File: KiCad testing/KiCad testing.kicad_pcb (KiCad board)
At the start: 2 copper layers, 29 parts, among them J1 USB_A, Q1 IRF540N, Q2 IRF540N, Q3 IRF540N, U1 IR2113S, U2 IR2113S, U3 ACS712xLCTR-05B

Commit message: Update Schematic
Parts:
- removed U2: IR2113S, Package_DIP:DIP-14_W7.62mm_Socket
- added C1: 10uF, Capacitor_THT:CP_Radial_D5.0mm_P2.00mm, F.Cu at (72.9, 149.9)
- added C2: 10uF, Capacitor_THT:CP_Radial_D5.0mm_P2.00mm, F.Cu at (61.5, 144.1)
- added C3: 100uF, Capacitor_THT:CP_Radial_D6.3mm_P2.50mm, F.Cu at (48.8, 140.2)
- added C4: 100nF, Capacitor_THT:C_Disc_D4.7mm_W2.5mm_P5.00mm, F.Cu at (45.1, 133.9)
- added C5: 10uF, Capacitor_THT:CP_Radial_D5.0mm_P2.00mm, F.Cu at (107.9, 151.1)
- added C6: 10uF, Capacitor_THT:CP_Radial_D5.0mm_P2.00mm, F.Cu at (95.9, 143.5)
- added C7: 100uF, Capacitor_THT:CP_Radial_D6.3mm_P2.50mm, F.Cu at (83.8, 139.7)
- added C8: 100nF, Capacitor_THT:C_Disc_D4.7mm_W2.5mm_P5.00mm, F.Cu at (80.7, 133.3)
- added U4: IR2213, Package_DIP:DIP-14_W7.62mm, F.Cu at (67.8, 129.5)
- U1: value IR2113S -> IR2213; footprint Package_DIP:DIP-14_W7.62mm_Socket -> Package_DIP:DIP-14_W7.62mm
- moved J1 149.3 mm to (49.7, 105.5), turned to -90 degrees
- moved R6 110.6 mm to (99.0, 148.6), turned to 180 degrees
- moved R3 108.1 mm to (64.0, 149.1), turned to 180 degrees
- moved C11 106.1 mm to (85.6, 160.0)
- moved C12 106.1 mm to (105.9, 162.5)
- moved D5 106.1 mm to (100.8, 167.7)
- moved L2 106.1 mm to (95.8, 161.3)
- moved Q1 106.1 mm to (98.3, 172.8)
- moved C9 103.6 mm to (71.6, 161.3)
- moved D3 103.6 mm to (56.4, 167.6)
- moved D4 103.6 mm to (70.3, 167.6)
- moved C10 103.6 mm to (51.1, 158.8)
- moved L1 103.6 mm to (62.7, 158.8)
- moved Q2 103.6 mm to (67.8, 172.7)
- moved Q3 103.6 mm to (53.8, 172.7)
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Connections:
- A1 pad 12: PWM_High -> PWM_Low
- A1 pad 13: PWM_Low -> PWM_High
- R1 pad 2: Net-(U1-LO) -> Net-(U4-LO)
- R3 pad 1: Net-(U1-HO) -> Net-(U4-HO)
- R4 pad 2: Net-(U2-LO) -> Net-(U1-LO)
- R6 pad 1: Net-(U2-HO) -> Net-(U1-HO)
- U1 pad 10: unconnected-(U1-NC-Pad10) -> PWM_MPPT
- U1 pad 11: 5V -> +Buck_Boost_Load
- U1 pad 12: PWM_High -> unconnected-(U1-LIN-Pad12)
- U1 pad 14: PWM_Low -> unconnected-(U1-NC-Pad14)
- U1 pad 5: unconnected-(U1-NC-Pad5) -> VS_1
- U1 pad 6: VS -> Net-(D2-K)
- U1 pad 7: Net-(D1-K) -> Net-(U1-HO)
- U1 pad 8: Net-(U1-HO) -> unconnected-(U1-NC-Pad8)
- U1 pad 9: unconnected-(U1-NC-Pad9) -> 5V
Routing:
- net +Buck_Boost_Load: track 60.7 -> 216.8 mm
- net 5V: track 0.00 -> 100.5 mm
- net 12V: track 7.86 -> 76.8 mm
- net PWM_MPPT: track 0.00 -> 37.4 mm
- net PWM_High: track 0.00 -> 28.1 mm
- net Gate_High: track 67.6 -> 39.5 mm
- net Gate_High_1: track 64.8 -> 38.2 mm
- net PWM_Low: track 0.00 -> 22.0 mm
- net Net-(D1-K): track 15.5 -> 33.3 mm
- net Net-(D2-K): track 15.2 -> 31.5 mm
- net VS_1: track 3.82 -> 12.0 mm
- net VS: track 48.3 -> 54.2 mm
- net Net-(U2-LO): track 5.25 -> 0.00 mm
- net Net-(U4-LO): track 0.00 -> 5.16 mm
- net Net-(U2-HO): track 3.80 -> 0.00 mm
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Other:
- board outline added: 101.6 x 127 mm
- board text added: "Cut outline marks the biggest pcb craftable."

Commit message: Update Schematic
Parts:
- C2, C6: value 10uF -> 470uF; footprint Capacitor_THT:CP_Radial_D5.0mm_P2.00mm -> Capacitor_THT:CP_Radial_D10.0mm_P5.00mm

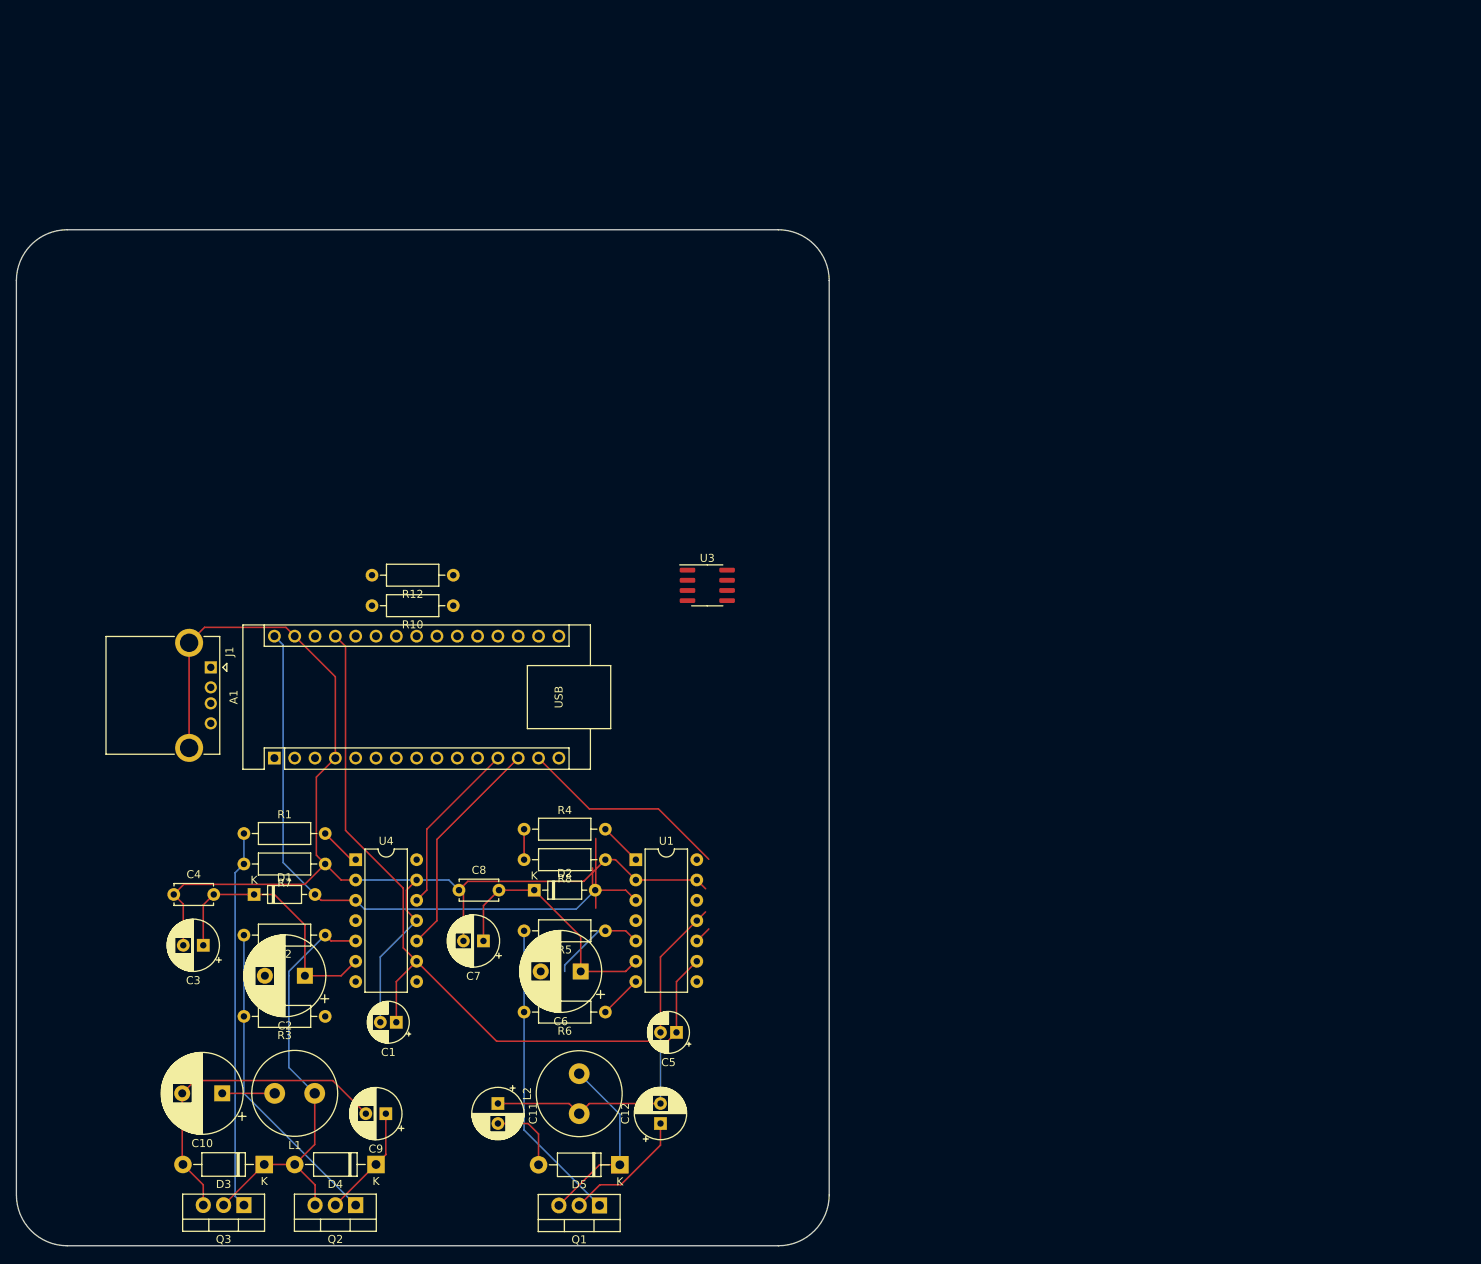
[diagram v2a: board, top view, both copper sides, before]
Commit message: Update schematic and redesign pcb layout.
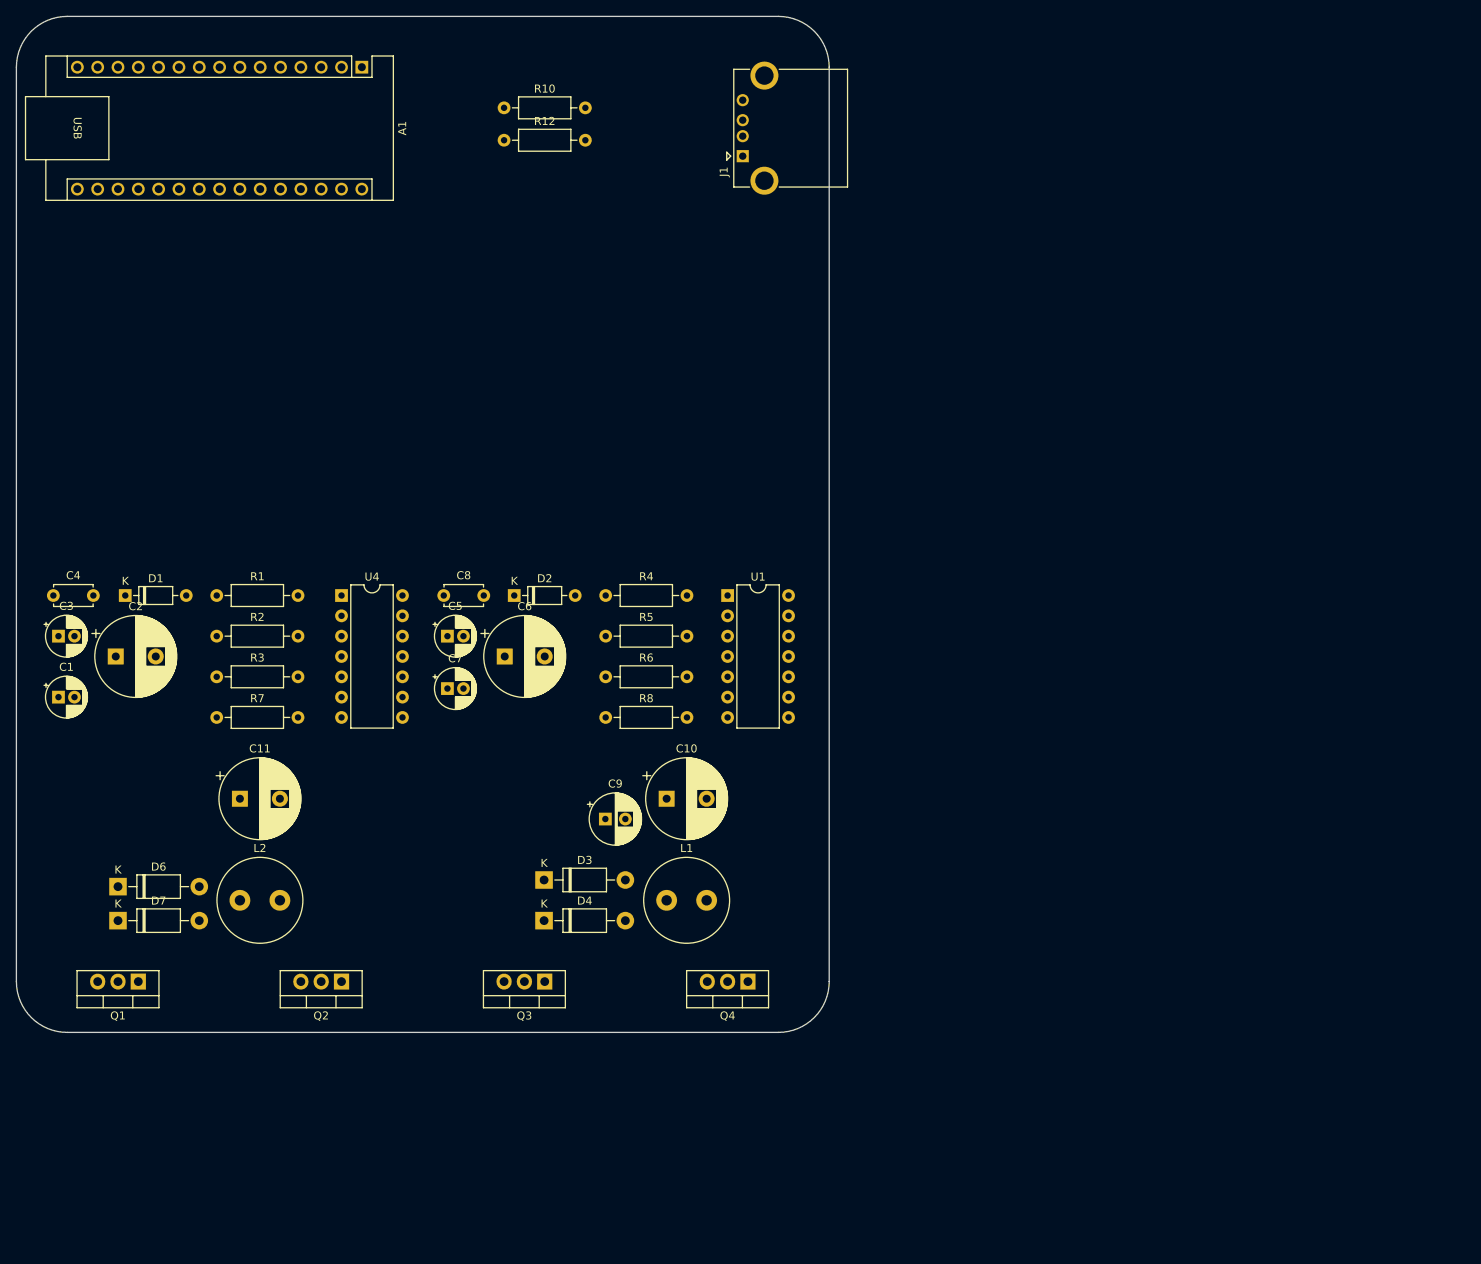
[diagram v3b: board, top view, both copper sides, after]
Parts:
- removed C12: 47uF, Capacitor_THT:CP_Radial_D6.3mm_P2.50mm
- removed D5: 1N4002, Diode_THT:D_DO-41_SOD81_P10.16mm_Horizontal
- removed U3: ACS712xLCTR-05B, Package_SO:SOIC-8_3.9x4.9mm_P1.27mm
- added D6: 1N4002, Diode_THT:D_DO-41_SOD81_P10.16mm_Horizontal, F.Cu at (38.1, 132.9)
- added D7: 1N4002, Diode_THT:D_DO-41_SOD81_P10.16mm_Horizontal, F.Cu at (38.1, 137.2)
- added Q4: IRF540N, Package_TO_SOT_THT:TO-220-3_Vertical, F.Cu at (116.8, 144.8)
- C11: value 47uF -> 1000uF; footprint Capacitor_THT:CP_Radial_D6.3mm_P2.50mm -> Capacitor_THT:CP_Radial_D10.0mm_P5.00mm
- C3, C7: footprint Capacitor_THT:CP_Radial_D6.3mm_P2.50mm -> Capacitor_THT:CP_Radial_D5.0mm_P2.00mm
- moved J1 92.2 mm to (116.2, 41.6), turned to 90 degrees
- moved A1 87.0 mm to (68.6, 30.5), turned to -90 degrees
- moved C10 66.7 mm to (106.7, 121.9), turned to 0 degrees
- moved Q1 64.1 mm to (40.6, 144.8)
- moved R10 62.6 mm to (86.4, 35.6), turned to 0 degrees
- moved C1 58.6 mm to (30.7, 109.2), turned to 0 degrees
- moved C5 57.2 mm to (79.3, 101.6), turned to 0 degrees
- moved R12 54.7 mm to (86.4, 39.6), turned to 0 degrees
- moved L1 50.2 mm to (106.7, 134.6), turned to 0 degrees
- moved L2 50.1 mm to (53.3, 134.6), turned to 0 degrees
- moved C11 49.9 mm to (53.3, 121.9), turned to 0 degrees
- moved D3 49.9 mm to (91.4, 132.1), turned to 0 degrees
- moved Q3 46.8 mm to (91.4, 144.8)
- moved C2 46.4 mm to (37.8, 104.1), turned to 0 degrees
- moved C9 45.9 mm to (99.0, 124.5), turned to 0 degrees
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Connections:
- A1 pad 29: +Buck_Boost_Load -> GND
- A1 pad 4: +Buck_Boost_Load -> GND
- C1 pad 2: +Buck_Boost_Load -> GND
- C11 pad 1: +Buck_Boost_Load -> -DCDC_Load
- C11 pad 2: -Buck_Boost_Load -> +DCDC_Load
- C3 pad 2: +Buck_Boost_Load -> GND
- C4 pad 1: +Buck_Boost_Load -> GND
- C5 pad 2: +Buck_Boost_Load -> GND
- C7 pad 2: +Buck_Boost_Load -> GND
- C8 pad 1: +Buck_Boost_Load -> GND
- J1 pad 5: +Buck_Boost_Load -> GND
- L2 pad 1: +Buck_Boost_Load -> Net-(D6-K)
- L2 pad 2: Net-(D5-K) -> Net-(D7-A)
- Q1 pad 3: Net-(D5-K) -> Net-(D6-K)
- Q2 pad 1: Gate_High -> Gate_Low_1
- Q2 pad 2: -Bidirectional_DCDC_Load -> Net-(D7-A)
- Q2 pad 3: VS -> -DCDC_Load
- Q3 pad 1: Gate_Low -> Gate_High
- Q3 pad 2: VS -> -Bidirectional_DCDC_Load
- Q3 pad 3: +Bidirectional_DCDC_Load -> VS
- R10 pad 2: +Buck_Boost_Load -> GND
- R12 pad 2: +Buck_Boost_Load -> GND
- R7 pad 1: +Buck_Boost_Load -> GND
- R8 pad 1: +Buck_Boost_Load -> GND
- U1 pad 11: +Buck_Boost_Load -> GND
- U1 pad 13: +Buck_Boost_Load -> GND
- U1 pad 2: +Buck_Boost_Load -> GND
- U4 pad 11: +Buck_Boost_Load -> GND
- U4 pad 13: +Buck_Boost_Load -> GND
- U4 pad 2: +Buck_Boost_Load -> GND
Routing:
- net +Buck_Boost_Load: track 216.8 -> 0.00 mm
- net 5V: track 100.5 -> 0.00 mm
- net 12V: track 76.8 -> 0.00 mm
- net VS: track 54.2 -> 0.00 mm
- net Gate_Low: track 47.4 -> 0.00 mm
- net +Bidirectional_DCDC_Load: track 40.4 -> 0.00 mm
- net Gate_High: track 39.5 -> 0.00 mm
- net Gate_High_1: track 38.2 -> 0.00 mm
- net PWM_MPPT: track 37.4 -> 0.00 mm
- net Net-(D1-K): track 33.3 -> 0.00 mm
- net Net-(D2-K): track 31.5 -> 0.00 mm
- net PWM_High: track 28.1 -> 0.00 mm
- net Net-(D5-K): track 23.2 -> 0.00 mm
- net PWM_Low: track 22.0 -> 0.00 mm
- net +PV: track 16.0 -> 0.00 mm
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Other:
- outline, holes or cut-outs redrawn

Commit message: update pcb
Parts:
- added ?: , , F.Cu at (121.9, 30.5)
- added ?: , , F.Cu at (30.5, 147.3)
- added ?: , , F.Cu at (30.5, 30.5)
- added REF**: MountingHole_3.2mm_M3_DIN965_Pad, MountingHole:MountingHole_3.2mm_M3_DIN965_Pad, F.Cu at (121.9, 30.5)
- added REF**: MountingHole_3.2mm_M3_DIN965_Pad, MountingHole:MountingHole_3.2mm_M3_DIN965_Pad, F.Cu at (30.5, 30.5)
- added REF**: MountingHole_3.2mm_M3_DIN965_Pad, MountingHole:MountingHole_3.2mm_M3_DIN965_Pad, F.Cu at (121.9, 147.3)
- added REF**: MountingHole_3.2mm_M3_DIN965_Pad, MountingHole:MountingHole_3.2mm_M3_DIN965_Pad, F.Cu at (30.5, 147.3)
- moved U1 80.1 mm to (36.8, 76.2), turned to 90 degrees
- moved C1 67.2 mm to (97.8, 111.6), turned to 90 degrees
- moved R8 65.9 mm to (40.6, 81.3), turned to -90 degrees
- moved R4 62.4 mm to (36.8, 91.4), turned to 90 degrees
- moved C3 60.3 mm to (90.2, 111.6), turned to 90 degrees
- moved C4 57.3 mm to (85.1, 112.2), turned to 90 degrees
- moved R5 55.5 mm to (44.5, 91.5), turned to 90 degrees
- moved C2 54.9 mm to (92.7, 104.4), turned to 90 degrees
- moved R7 53.7 mm to (100.3, 91.8), turned to 90 degrees
- moved R6 53.0 mm to (48.3, 91.5), turned to 90 degrees
- moved D2 51.0 mm to (36.8, 101.6), turned to 90 degrees
- moved R3 47.2 mm to (95.2, 91.8), turned to 90 degrees
- moved D1 46.6 mm to (85.1, 103.2), turned to 90 degrees
- moved C8 44.2 mm to (36.8, 110.5), turned to 90 degrees
- moved C6 42.1 mm to (44.5, 101.4), turned to 90 degrees
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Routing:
- net Net-(D2-K): track 0.00 -> 47.2 mm
- net 5V: track 0.00 -> 39.6 mm
- net Gate_High_1: track 0.00 -> 37.0 mm
- net Gate_Low_1: track 0.00 -> 25.4 mm
- net VS_1: track 0.00 -> 22.2 mm
- net 12V: track 0.00 -> 19.9 mm
- net GND: track 0.00 -> 19.4 mm
- net Net-(U1-HO): track 0.00 -> 16.8 mm
- net Net-(U1-LO): track 0.00 -> 5.07 mm
- added copper zone on B.Cu, net GND

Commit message: Update PCB
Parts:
- moved U1 48.3 mm to (36.8, 124.5), turned to 180 degrees
- moved U4 45.9 mm to (115.6, 110.5), turned to 0 degrees
- moved R8 39.4 mm to (41.9, 120.7), turned to 0 degrees
- moved C8 37.0 mm to (71.1, 124.5), turned to 180 degrees
- moved R4 36.4 mm to (52.1, 124.5), turned to 180 degrees
- moved D2 34.2 mm to (62.2, 124.5), turned to 180 degrees
- moved R3 30.5 mm to (100.3, 121.9), turned to 0 degrees
- moved R2 28.2 mm to (100.3, 118.1), turned to 0 degrees
- moved C7 27.0 mm to (67.9, 118.1), turned to 0 degrees
- moved R5 26.5 mm to (52.1, 116.8), turned to 180 degrees
- moved R7 24.7 mm to (110.5, 114.3), turned to 180 degrees
- moved R1 24.1 mm to (100.3, 110.5), turned to 0 degrees
- moved C6 23.4 mm to (62.1, 116.8), turned to 180 degrees
- moved L2 23.0 mm to (44.5, 135.9)
- moved C10 22.8 mm to (114.4, 135.9)
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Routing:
- net Net-(D1-K): track 0.00 -> 47.1 mm
- net -DCDC_Load: track 0.00 -> 46.8 mm
- net 5V: track 39.6 -> 79.3 mm
- net Gate_High: track 0.00 -> 37.1 mm
- net +DCDC_Load: track 0.00 -> 32.5 mm
- net Gate_Low: track 0.00 -> 25.4 mm
- net Net-(D7-A): track 0.00 -> 24.9 mm
- net Net-(D6-K): track 0.00 -> 22.4 mm
- net VS: track 0.00 -> 22.3 mm
- net 12V: track 19.9 -> 39.8 mm
- net GND: track 19.4 -> 0.00 mm
- net Net-(U4-HO): track 0.00 -> 16.8 mm
- net Gate_Low_1: track 25.4 -> 39.8 mm
- net Gate_High_1: track 37.0 -> 44.3 mm
- net Net-(U4-LO): track 0.00 -> 5.08 mm
